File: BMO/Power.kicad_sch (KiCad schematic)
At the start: 61 parts, among them J10 USB_C_Receptacle_USB2.0_16P, J11 BAT, Q1 MMDT2907A-7-F, Q2 DMP1045U-7, Q3 DMN313DLT-7, SW3 nQON, U4 USBLC6-2SC6, U5 AP2112K-3.3, U6 BQ27220YZFR, U7 BQ25896RTW

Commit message: feat(pcb): complete initial routing (v1) pending verification
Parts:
- added R13, R15: 1k5, Resistor_SMD:R_0402_1005Metric, symbol Device:R
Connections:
- net +3.3V: now also R13.1, R15.1
- net CHARG_SCL: now also R15.2
- net CHARG_SDA: now also R13.2

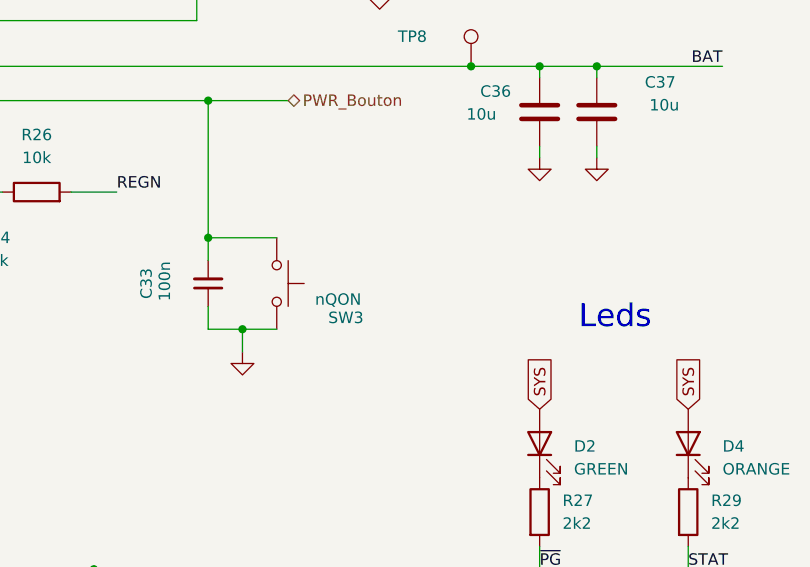
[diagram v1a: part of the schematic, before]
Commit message: added on/off button, CSV completed and pcb updated
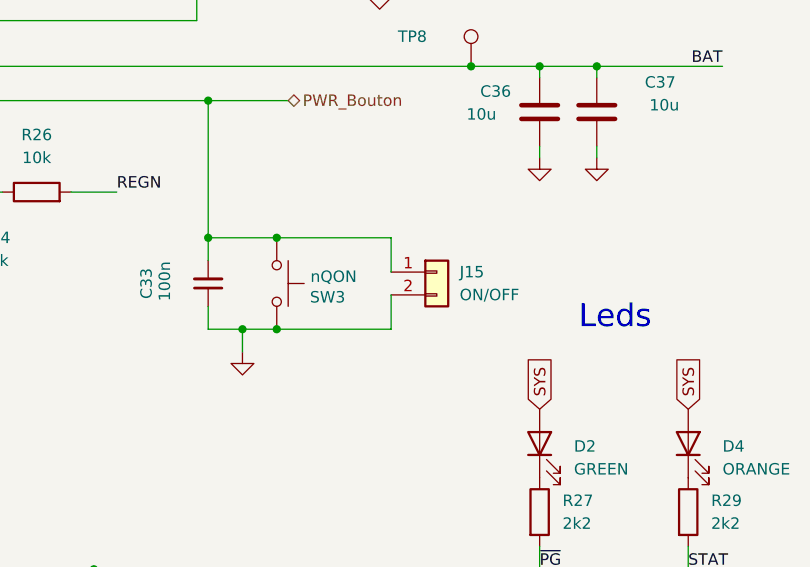
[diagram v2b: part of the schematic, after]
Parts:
- added J15: ON/OFF, Connector_JST:JST_XH_S2B-XH-A-1_1x02_P2.50mm_Horizontal, symbol Connector_Generic:Conn_01x02
- J11: JLCPCB Part # (none) -> C163035
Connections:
- net GND: now also J15.2 (Pin_2)
- net PWR_Bouton: now also J15.1 (Pin_1)

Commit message: Finalize PCB design and generate BOM and CPL files
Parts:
- removed R13, R15: 1k5, Resistor_SMD:R_0402_1005Metric, symbol Device:R
- VBAT1: renamed from TP8; footprint TestPoint:TestPoint_Pad_D2.0mm -> TestPoint:TestPoint_Pad_D1.5mm
- renumbered TP7 to 3V3, TP5 to 5V1, C24 to C25, C25 to C26, C26 to C27, C27 to C28, C28 to C29, C29 to C30, C30 to C31, C31 to C32, C32 to C33, C33 to C34, C34 to C35, C35 to C36, C36 to C37, C37 to C38, J15 to J12, R14 to R13, R16 to R14, R17 to R15, R18 to R16, R19 to R17, R20 to R18, R21 to R19, R22 to R20, R23 to R21, R24 to R22, R25 to R23, R26 to R24, R27 to R25, R28 to R26, R29 to R27, R30 to R28, TP9 to SYS1, TP11 to TP4, TP4 to TP5, TP6 to VBUS1

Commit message: Update USB-C connector to in-stock part, align CPL coordinates and finalize BOM
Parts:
- J10: JLCPCB Part # C3020560 -> C5184243
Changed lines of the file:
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@@
 			)
 		)
-		(property "JLCPCB Part #" "C3020560"
+		(property "JLCPCB Part #" "C5184243"
 			(at 39.37 55.88 0)
 			(hide yes)
